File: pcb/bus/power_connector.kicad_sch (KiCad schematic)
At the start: 3 parts, among them J201 Conn_02x10_Row_Letter_First

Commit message: update bus pcb
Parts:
- removed H201, H202: MountingHole_Pad, MountingHole:MountingHole_3.2mm_M3_Pad_Via, symbol Mechanical:MountingHole_Pad
- removed J201: Conn_02x10_Row_Letter_First, PRJ:PCN10-20P-2.54DSA, symbol Connector_Generic:Conn_02x10_Row_Letter_First
- added H301, H302: MountingHole_Pad, MountingHole:MountingHole_3.2mm_M3_Pad_Via, symbol Mechanical:MountingHole_Pad
- added J301: Conn_02x10_Row_Letter_First, PRJ:PCN10-20P-2.54DSA, symbol Connector_Generic:Conn_02x10_Row_Letter_First
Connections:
- net +12V: now also J301.a10 (Pin_a10), J301.a9 (Pin_a9), J301.b10 (Pin_b10), J301.b9 (Pin_b9)
- net +5V: now also J301.a6 (Pin_a6), J301.a7 (Pin_a7), J301.b6 (Pin_b6), J301.b7 (Pin_b7)
- net GND: now also H301.1, H302.1, J301.a1 (Pin_a1), J301.a8 (Pin_a8), J301.b1 (Pin_b1), J301.b8 (Pin_b8)
- net I2C_SCL: now also J301.a2 (Pin_a2)
- net I2C_SDA: now also J301.a3 (Pin_a3)
- no-connect marks 4 -> 6
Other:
- title: Bus Connector -> (none)

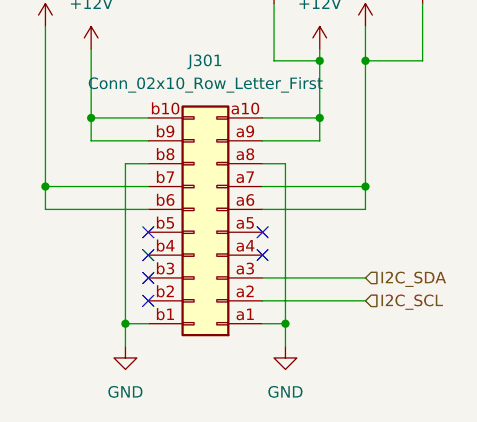
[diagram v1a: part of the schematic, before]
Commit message: power pin fix
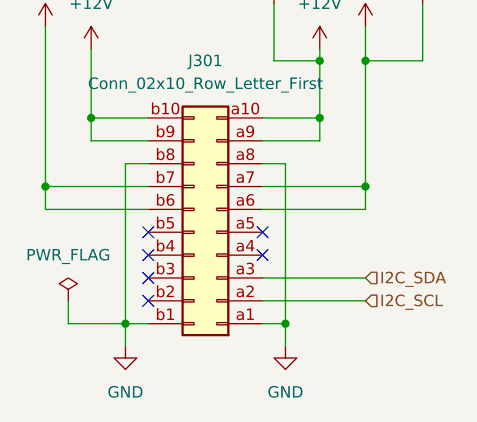
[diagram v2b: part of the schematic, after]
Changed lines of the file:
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@@
+		)
+	)
+	(wire
+		(pts
+			(xy 133.35 99.06) (xy 133.35 101.6)
+		)
+		(stroke
+			(width 0)
+			(type default)
+		)
+	)
+	(wire
+		(pts
+			(xy 133.35 101.6) (xy 139.7 101.6)
+		)
+		(stroke
+			(width 0)
+			(type default)
 		)
 	)
@@
 					(unit 1)
 				)
+			)
+		)
+	)
+	(symbol
+		(lib_id "power:PWR_FLAG")
+		(at 133.35 99.06 0)
+		(unit 1)
+		(exclude_from_sim no)
+		(in_bom yes)
+		(on_board yes)
+		(dnp no)
+		(fields_autoplaced yes)
+		(property "Reference" "#FLG0303"
+			(at 133.35 97.155 0)
+			(effects
+				(font
+					(size 1.27 1.27)
+				)
+				(hide yes)
+			)
+		)
+		(property "Value" "PWR_FLAG"
+			(at 133.35 93.98 0)
+			(effects
+				(font
+					(size 1.27 1.27)
+				)
+			)
+		)
+		(property "Footprint" ""
+			(at 133.35 99.06 0)
+			(effects
+				(font
+					(size 1.27 1.27)
+				)
+				(hide yes)
+			)
+		)
+		(property "Datasheet" "~"
+			(at 133.35 99.06 0)
+			(effects
+				(font
+					(size 1.27 1.27)
+				)
+				(hide yes)
+			)
+		)
+		(property "Description" "Special symbol for telling ERC where power comes from"
+			(at 133.35 99.06 0)
+			(effects
+				(font
+					(size 1.27 1.27)
+				)
+				(hide yes)
+			)
+		)
+		(pin "1"
+		)
+		(instances
+			(project "bus"
+				(path "/5d20b266-567e-45c6-9e3e-145c2aea1daa/4945f18d-16f7-4109-826d-838a95062554"
+					(reference "#FLG0303")
+					(unit 1)
+				)

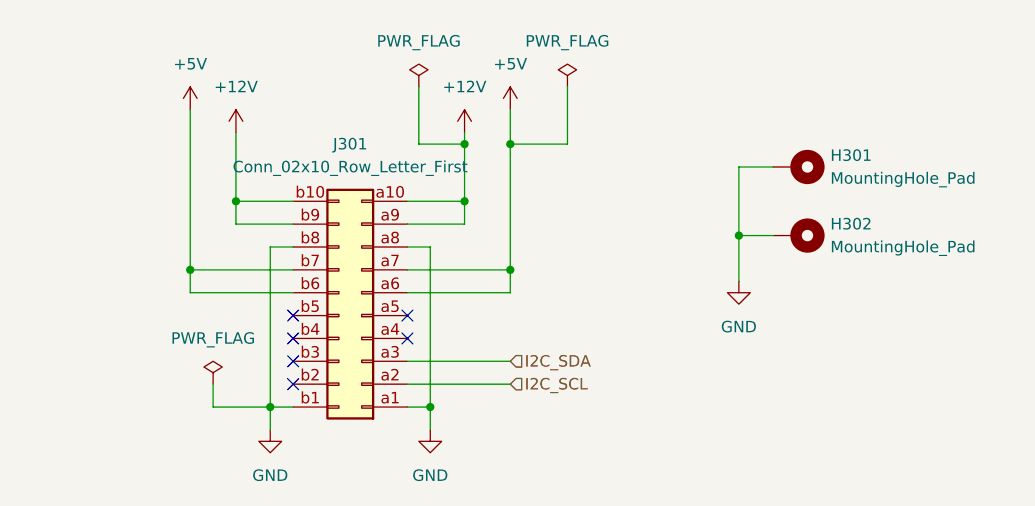
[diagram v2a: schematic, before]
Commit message: update pcb size
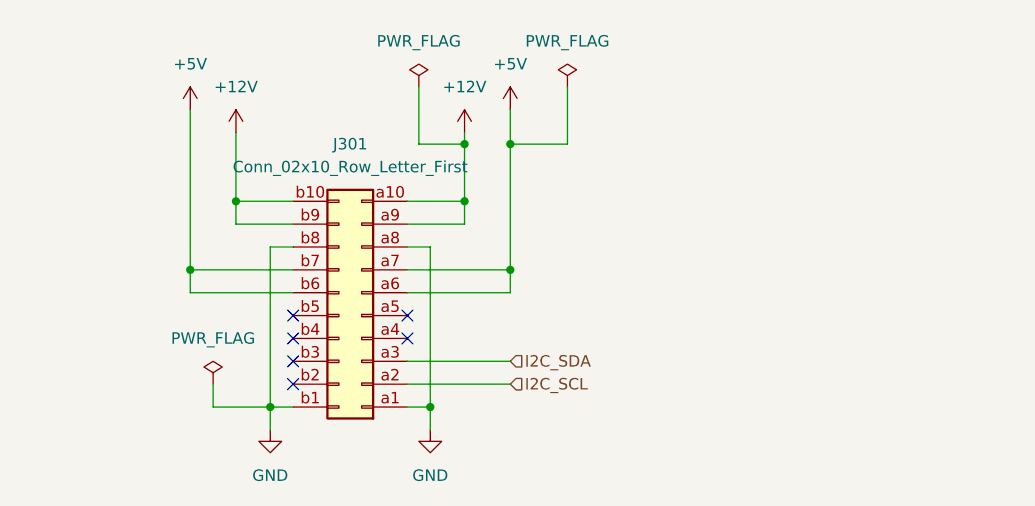
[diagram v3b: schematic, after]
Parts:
- removed H301, H302: MountingHole_Pad, MountingHole:MountingHole_3.2mm_M3_Pad_Via, symbol Mechanical:MountingHole_Pad

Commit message: update bus pcb
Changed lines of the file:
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@@
 	)
 	(hierarchical_label "I2C_SDA"
-		(shape input)
+		(shape bidirectional)
 		(at 166.37 96.52 0)
 		(effects
@@
 	)
 	(hierarchical_label "I2C_SCL"
-		(shape input)
+		(shape bidirectional)
 		(at 166.37 99.06 0)
 		(effects

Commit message: update ALL parts
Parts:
- J301: MOUSER (none) -> 798-PCN1020P254DSA72
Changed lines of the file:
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@@
+			)
+		)
+		(property "MOUSER" "798-PCN1020P254DSA72"
+			(at 149.86 91.44 0)
+			(effects
+				(font
+					(size 1.27 1.27)
+				)
+				(hide yes)
 			)
 		)
